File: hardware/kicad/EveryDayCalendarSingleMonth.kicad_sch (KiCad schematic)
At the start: 143 parts, among them J1_ONE_WIRE1 Conn_01x03, J2_POWER_IN1 Conn_01x02, J3_PROGRAMING_PIN1 Conn_01x06, Q1_PROGRAMING1 PN2222A, Q2_PROGRAMING1 PN2222A, U1 74AHC1G125

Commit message: Working on getting all the traces done
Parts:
- removed C12, C3: 1uF,25V,X5R, tom-passives:C_0402_1005Metric, symbol jlcpcb-basic-capacitor-0402:1uF,25V,X5R
- removed TP1_IO1: TestPoint, TestPoint:TestPoint_Pad_D2.0mm, symbol Connector:TestPoint
- added SW_WIN2: Switch_SW_Push, calendar:SW_Push_1P1T_NO_6x6mm_H9.5mm, symbol tom-mechanical:SW_SPST
- added TP_LEDLINK_IN1: TestPoint, TestPoint:TestPoint_Pad_2.5x2.5mm, symbol Connector:TestPoint
- renumbered C20 to C19, C21 to C20, C22 to C21, C23 to C22, C24 to C23, C25 to C24, C26 to C25, C27 to C26, C28 to C27, C29 to C28, C30 to C29, C31 to C30, C32 to C31, C33 to C32, C34 to C33, C35 to C34, C36 to C35, C37 to C36, C38 to C37, C39 to C38, C40 to C39, C41 to C40, C42 to C41, C43 to C42, C50 to C43, D19 to D1, D1 to DAY1, D10 to DAY10, D11 to DAY11, D12 to DAY12, D13 to DAY13, D14 to DAY14, D15 to DAY15, D16 to DAY16, D17 to DAY17, D18 to DAY18, D20 to DAY19, D2 to DAY2, D21 to DAY20, D22 to DAY21, D23 to DAY22, D24 to DAY23, D25 to DAY24, D26 to DAY25, D27 to DAY26, D28 to DAY27, D29 to DAY28, D30 to DAY29, D3 to DAY3, D31 to DAY30, D32 to DAY31, D33 to DAY32, D34 to DAY33, D35 to DAY34, D36 to DAY35, D37 to DAY36, D38 to DAY37, D39 to DAY38, D40 to DAY39, D4 to DAY4, D41 to DAY40, D42 to DAY41, D43 to DAY42, D5 to DAY5, D6 to DAY6, D7 to DAY7, D8 to DAY8, D9 to DAY9, TP_CORNER_3 to TP_CORNER_2, TP_CORNER_4 to TP_CORNER_3, TP_CORNER_2 to TP_CORNER_4, TP1 to TP_LEDLINK_OUT1
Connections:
- net PIN_TEST_POINT is gone; now on net WEEK1: U_CPU1.26 (IO4)
- net DAY1: now also U_CPU1.13 (IO14); no longer U_CPU1.29 (IO5)
- net DAY2: now also U_CPU1.23 (IO15); no longer U_CPU1.14 (IO12)
- net DAY3: now also U_CPU1.33 (IO21); no longer U_CPU1.13 (IO14)
- net DAY4: now also U_CPU1.36 (IO22); no longer U_CPU1.23 (IO15)
- net DAY5: now also U_CPU1.37 (IO23); no longer U_CPU1.27 (IO16)
- net DAY6: now also U_CPU1.10 (IO25); no longer U_CPU1.28 (IO17)
- net DAY7: now also U_CPU1.11 (IO26); no longer U_CPU1.30 (IO18)
- net GND: now also SW_WIN2.1 (A)
- net PIN_LED_CAL: now also U_CPU1.14 (IO12); no longer U_CPU1.9 (IO33)
- net WEEK1: no longer U_CPU1.31 (IO19)
- net WEEK2: now also U_CPU1.27 (IO16); no longer U_CPU1.33 (IO21)
- net WEEK3: now also U_CPU1.28 (IO17); no longer U_CPU1.36 (IO22)
- net WEEK4: now also U_CPU1.29 (IO5); no longer U_CPU1.37 (IO23)
- net WEEK5: now also U_CPU1.31 (IO19); no longer U_CPU1.10 (IO25)
- net WEEK6: now also U_CPU1.30 (IO18); no longer U_CPU1.11 (IO26)
- net at D_S1.3 (DIN): now also DAY42.1 (DOUT); no longer U1.4
- net at DAY1.3 (DIN): now also U1.4; no longer D_S3.1 (DOUT)
- net at TP_LEDLINK_OUT1.1: now also D_S3.1 (DOUT); no longer DAY42.1 (DOUT)
- net BUTTON_WIN renamed BUTTON_WIN1
- net LED_LINK: no longer names the net of R1.2, U1.2
- net LED_LINK: now also TP_LEDLINK_IN1.1
- new net BUTTON_WIN2: SW_WIN2.2 (B), U_CPU1.9 (IO33)
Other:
- moved on the sheet: C13, C14, C15, C16, C17, C18, C19, C20, C21, C22, C23, C24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

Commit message: added GND base
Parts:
- removed TP_CORNER_1, TP_CORNER_2, TP_CORNER_3, TP_CORNER_4: TestPoint, MountingHole:MountingHole_3.2mm_M3, symbol Connector:TestPoint
- renumbered SW_RESET_PROGRAMING1 to SW_BOOTLOAD1
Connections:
- net VCC is gone; now on net +5V: U1.5 (VCC)
- net RESET: now also SW_RESET1.1 (A)
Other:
- note removed: "TODO: Fix power to U2"

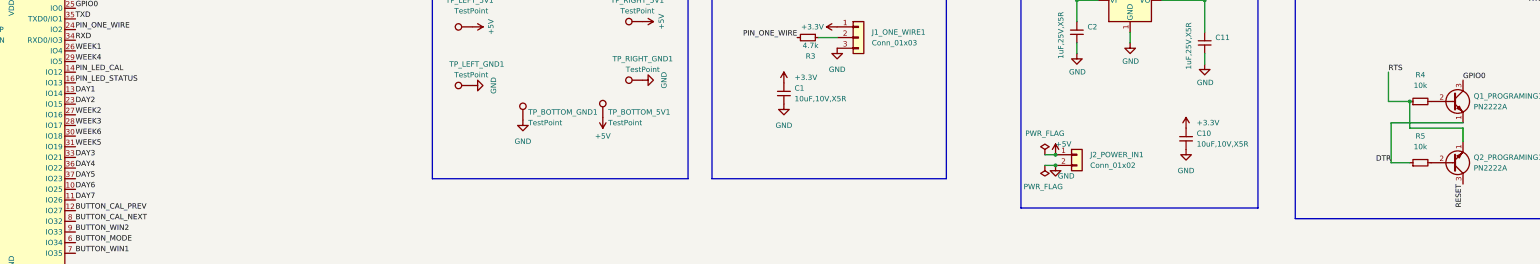
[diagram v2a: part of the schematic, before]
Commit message: Added 3d part for pushbuttons
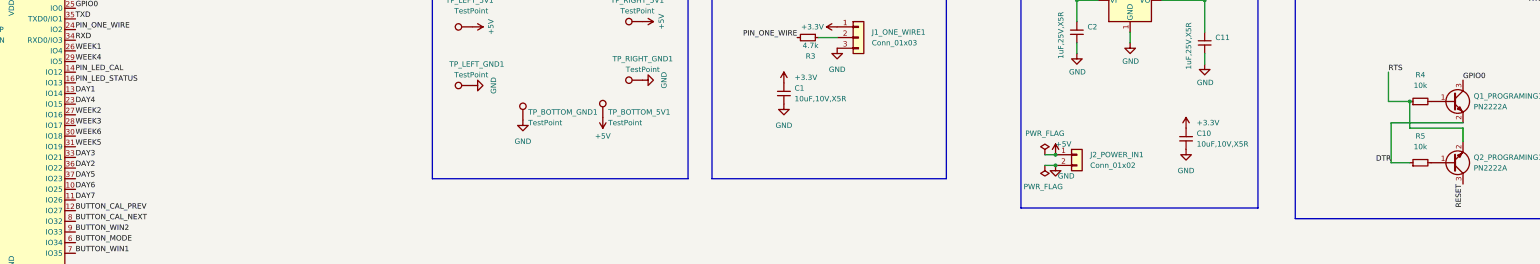
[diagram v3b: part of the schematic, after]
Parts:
- Q1_PROGRAMING1, Q2_PROGRAMING1: symbol Transistor_BJT:PN2222A -> Transistor_BJT:MMBT3904
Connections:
- net DAY2: now also U_CPU1.36 (IO22); no longer U_CPU1.23 (IO15)
- net DAY4: now also U_CPU1.23 (IO15); no longer U_CPU1.36 (IO22)
- net DTR: now also Q1_PROGRAMING1.2 (E); no longer Q1_PROGRAMING1.1 (E)
- net RTS: now also Q2_PROGRAMING1.2 (E); no longer Q2_PROGRAMING1.1 (E)
- net at R4.2: now also Q1_PROGRAMING1.1 (B); no longer Q1_PROGRAMING1.2 (B)
- net at R5.2: now also Q2_PROGRAMING1.1 (B); no longer Q2_PROGRAMING1.2 (B)
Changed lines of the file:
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@@
     (effects (font (size 1.27 1.27)) (justify left bottom))
   )
-  (label "DAY4" (at 137.795 104.775 0)
+  (label "DAY4" (at 137.795 89.535 0)
     (effects (font (size 1.27 1.27)) (justify left bottom))
   )
@@
     (effects (font (size 1.27 1.27)) (justify left bottom))
   )
-  (label "DAY2" (at 137.795 89.535 0)
+  (label "DAY2" (at 137.795 104.775 0)
     (effects (font (size 1.27 1.27)) (justify left bottom))
   )
@@
     (pin "4")
   )
-  (symbol (lib_id "Transistor_BJT:PN2222A") (at 466.09 103.505 0) (mirror x) (unit 1)
+  (symbol (lib_id "Transistor_BJT:MMBT3904") (at 466.09 103.505 0) (mirror x) (unit 1)
     (in_bom yes) (on_board yes) (fields_autoplaced)
     (property "Reference" "Q2_PROGRAMING1" (id 0) (at 471.17 102.2349 0)
@@
       (effects (font (size 1.27 1.27) italic) (justify left) hide)
     )
-    (property "Datasheet" "https://www.onsemi.com/pub/Collateral/PN2222-D.PDF" (id 3) (at 466.09 103.505 0)
+    (property "Datasheet" "https://www.onsemi.com/pub/Collateral/2N3903-D.PDF" (id 3) (at 466.09 103.505 0)
       (effects (font (size 1.27 1.27)) (justify left) hide)
     )
@@
     (pin "1")
   )
-  (symbol (lib_id "Transistor_BJT:PN2222A") (at 466.09 88.9 0) (unit 1)
+  (symbol (lib_id "Transistor_BJT:MMBT3904") (at 466.09 88.9 0) (unit 1)
     (in_bom yes) (on_board yes) (fields_autoplaced)
     (property "Reference" "Q1_PROGRAMING1" (id 0) (at 471.17 87.6299 0)
@@
       (effects (font (size 1.27 1.27) italic) (justify left) hide)
     )
-    (property "Datasheet" "https://www.onsemi.com/pub/Collateral/PN2222-D.PDF" (id 3) (at 466.09 88.9 0)
+    (property "Datasheet" "https://www.onsemi.com/pub/Collateral/2N3903-D.PDF" (id 3) (at 466.09 88.9 0)
       (effects (font (size 1.27 1.27)) (justify left) hide)
     )

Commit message: Zero errors or warnings.
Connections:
- net +3.3V: no longer C1.1, J1_ONE_WIRE1.1 (Pin_1)
- net +5V: now also C1.1, J1_ONE_WIRE1.1 (Pin_1)
- net BUTTON_CAL_NEXT: now also U_CPU1.6 (IO34); no longer U_CPU1.8 (IO32)
- net BUTTON_CAL_PREV: now also U_CPU1.7 (IO35); no longer U_CPU1.12 (IO27)
- net BUTTON_MODE: now also U_CPU1.8 (IO32); no longer U_CPU1.6 (IO34)
- net BUTTON_WIN1: now also U_CPU1.11 (IO26); no longer U_CPU1.7 (IO35)
- net DAY1: now also U_CPU1.37 (IO23); no longer U_CPU1.13 (IO14)
- net DAY5: now also U_CPU1.14 (IO12); no longer U_CPU1.37 (IO23)
- net DAY6: now also U_CPU1.13 (IO14); no longer U_CPU1.10 (IO25)
- net DAY7: now also U_CPU1.12 (IO27); no longer U_CPU1.11 (IO26)
- net PIN_LED_CAL: now also U_CPU1.10 (IO25); no longer U_CPU1.14 (IO12)
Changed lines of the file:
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@@
     (effects (font (size 1.27 1.27)) (justify left bottom))
   )
-  (label "BUTTON_CAL_NEXT" (at 137.795 117.475 0)
+  (label "BUTTON_CAL_NEXT" (at 137.795 122.555 0)
     (effects (font (size 1.27 1.27)) (justify left bottom))
   )
@@
     (effects (font (size 1.27 1.27)) (justify left bottom))
   )
-  (label "DAY5" (at 137.795 107.315 0)
+  (label "DAY5" (at 137.795 81.915 0)
     (effects (font (size 1.27 1.27)) (justify left bottom))
   )
@@
     (effects (font (size 1.27 1.27)) (justify right bottom))
   )
-  (label "DAY6" (at 137.795 109.855 0)
+  (label "DAY6" (at 137.795 86.995 0)
     (effects (font (size 1.27 1.27)) (justify left bottom))
   )
@@
     (effects (font (size 1.27 1.27)) (justify left bottom))
   )
-  (label "BUTTON_WIN1" (at 137.795 125.095 0)
+  (label "BUTTON_WIN1" (at 137.795 112.395 0)
     (effects (font (size 1.27 1.27)) (justify left bottom))
   )
@@
     (effects (font (size 1.27 1.27)) (justify left bottom))
   )
-  (label "BUTTON_MODE" (at 137.795 122.555 0)
+  (label "BUTTON_MODE" (at 137.795 117.475 0)
     (effects (font (size 1.27 1.27)) (justify left bottom))
   )
-  (label "DAY1" (at 137.795 86.995 0)
+  (label "DAY1" (at 137.795 107.315 0)
     (effects (font (size 1.27 1.27)) (justify left bottom))
   )
@@
     (effects (font (size 1.27 1.27)) (justify right bottom))
   )
-  (label "DAY7" (at 137.795 112.395 0)
+  (label "DAY7" (at 137.795 114.935 0)
     (effects (font (size 1.27 1.27)) (justify left bottom))
   )
@@
     (effects (font (size 1.27 1.27)) (justify right bottom))
   )
-  (label "BUTTON_CAL_PREV" (at 137.795 114.935 0)
+  (label "BUTTON_CAL_PREV" (at 137.795 125.095 0)
     (effects (font (size 1.27 1.27)) (justify left bottom))
   )
-  (label "PIN_LED_CAL" (at 137.795 81.915 0)
+  (label "PIN_LED_CAL" (at 137.795 109.855 0)
     (effects (font (size 1.27 1.27)) (justify left bottom))
   )
@@
     (pin "1")
   )
-  (symbol (lib_id "power:+3.3V") (at 319.405 71.12 90) (unit 1)
-    (in_bom yes) (on_board yes) (fields_autoplaced)
-    (property "Reference" "#PWR010" (id 0) (at 323.215 71.12 0)
-      (effects (font (size 1.27 1.27)) hide)
-    )
-    (property "Value" "+3.3V" (id 1) (at 316.23 71.1199 90)
-      (effects (font (size 1.27 1.27)) (justify left))
-    )
-    (property "Footprint" "" (id 2) (at 319.405 71.12 0)
-      (effects (font (size 1.27 1.27)) hide)
-    )
-    (property "Datasheet" "" (id 3) (at 319.405 71.12 0)
-      (effects (font (size 1.27 1.27)) hide)
-    )
-    (pin "1")
-  )
   (symbol (lib_id "calendar:WS2812B") (at 243.84 238.125 0) (unit 1)
     (in_bom yes) (on_board yes) (fields_autoplaced)
@@
     (pin "3")
   )
+  (symbol (lib_id "power:+5V") (at 306.705 84.455 0) (unit 1)
+    (in_bom yes) (on_board yes) (fields_autoplaced)
+    (property "Reference" "#PWR08" (id 0) (at 306.705 88.265 0)
+      (effects (font (size 1.27 1.27)) hide)
+    )
+    (property "Value" "+5V" (id 1) (at 306.705 79.375 0))
+    (property "Footprint" "" (id 2) (at 306.705 84.455 0)
+      (effects (font (size 1.27 1.27)) hide)
+    )
+    (property "Datasheet" "" (id 3) (at 306.705 84.455 0)
+      (effects (font (size 1.27 1.27)) hide)
+    )
+    (pin "1")
+  )
   (symbol (lib_id "tom-mechanical:SW_SPST") (at 38.1 71.12 0) (unit 1)
     (in_bom yes) (on_board yes)
@@
     (pin "2")
   )
+  (symbol (lib_id "power:+5V") (at 319.405 71.12 0) (unit 1)
+    (in_bom yes) (on_board yes) (fields_autoplaced)
+    (property "Reference" "#PWR010" (id 0) (at 319.405 74.93 0)
+      (effects (font (size 1.27 1.27)) hide)
+    )
+    (property "Value" "+5V" (id 1) (at 319.405 66.04 0))
+    (property "Footprint" "" (id 2) (at 319.405 71.12 0)
+      (effects (font (size 1.27 1.27)) hide)
+    )
+    (property "Datasheet" "" (id 3) (at 319.405 71.12 0)
+      (effects (font (size 1.27 1.27)) hide)
+    )
+    (pin "1")
+  )
   (symbol (lib_id "calendar:WS2812B") (at 193.04 194.945 0) (unit 1)
     (in_bom yes) (on_board yes) (fields_autoplaced)
@@
     (pin "1")
   )
-  (symbol (lib_id "power:+3.3V") (at 306.705 84.455 0) (unit 1)
-    (in_bom yes) (on_board yes) (fields_autoplaced)
-    (property "Reference" "#PWR08" (id 0) (at 306.705 88.265 0)
-      (effects (font (size 1.27 1.27)) hide)
-    )
-    (property "Value" "+3.3V" (id 1) (at 309.245 83.1849 0)
-      (effects (font (size 1.27 1.27)) (justify left))
-    )
-    (property "Footprint" "" (id 2) (at 306.705 84.455 0)
-      (effects (font (size 1.27 1.27)) hide)
-    )
-    (property "Datasheet" "" (id 3) (at 306.705 84.455 0)
-      (effects (font (size 1.27 1.27)) hide)
-    )
-    (pin "1")
-  )
   (symbol (lib_id "power:+3.3V") (at 532.13 103.505 0) (unit 1)
     (in_bom yes) (on_board yes) (fields_autoplaced)
@@
       (reference "#PWR07") (unit 1) (value "GND") (footprint "")
     )
-    (path "/ef50650b-f40e-490b-b982-9f1bf0858617"
-      (reference "#PWR08") (unit 1) (value "+3.3V") (footprint "")
+    (path "/d2220ca1-4a38-4f7e-9c73-e0b2c3831917"
+      (reference "#PWR08") (unit 1) (value "+5V") (footprint "")
     )
     (path "/67f5eb89-5a5c-4633-8502-1c1dd8c84ae3"
       (reference "#PWR09") (unit 1) (value "GND") (footprint "")
     )
-    (path "/c3bbb8f7-f74d-4bf2-b28f-3f9ca4cf3c15"
-      (reference "#PWR010") (unit 1) (value "+3.3V") (footprint "")
+    (path "/d4519b1b-f257-451e-827a-277f5ee80280"
+      (reference "#PWR010") (unit 1) (value "+5V") (footprint "")
     )
     (path "/b35a029b-6727-4ae4-bcd0-21bab0a3bb4a"

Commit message: Updated silkscreen
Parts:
- renumbered TP_BOTTOM_5V1 to 5V, TP_RIGHT_5V1 to 5V, TP_LEFT_5V1 to 5V, SW_CAL_NEXT1 to CAL_NEXT, TP_BOTTOM_GND1 to GND, TP_LEDLINK_IN1 to LED_IN, TP_LEDLINK_OUT1 to LED_OUT, J1_ONE_WIRE1 to ONE_WIRE, Q1_PROGRAMING1 to Q1, Q2_PROGRAMING1 to Q2
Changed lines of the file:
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@@
   (symbol (lib_id "tom-mechanical:SW_SPST") (at 36.195 236.855 0) (unit 1)
     (in_bom yes) (on_board yes)
-    (property "Reference" "SW_CAL_NEXT1" (id 0) (at 36.195 231.14 0))
+    (property "Reference" "CAL_NEXT" (id 0) (at 36.195 231.14 0))
     (property "Value" "Switch_SW_Push" (id 1) (at 36.195 233.4514 0))
     (property "Footprint" "calendar:SW_Push_1P1T_NO_6x6mm_H9.5mm" (id 2) (at 36.195 231.775 0)
@@
   (symbol (lib_id "Transistor_BJT:MMBT3904") (at 466.09 103.505 0) (mirror x) (unit 1)
     (in_bom yes) (on_board yes) (fields_autoplaced)
-    (property "Reference" "Q2_PROGRAMING1" (id 0) (at 471.17 102.2349 0)
+    (property "Reference" "Q2" (id 0) (at 471.17 102.2349 0)
       (effects (font (size 1.27 1.27)) (justify left))
     )
@@
   (symbol (lib_id "Connector:TestPoint") (at 263.525 92.71 0) (unit 1)
     (in_bom yes) (on_board yes)
-    (property "Reference" "TP_BOTTOM_5V1" (id 0) (at 264.795 91.44 0)
+    (property "Reference" "5V" (id 0) (at 264.795 91.44 0)
       (effects (font (size 1.27 1.27)) (justify left))
     )
@@
   (symbol (lib_id "Connector:TestPoint") (at 273.05 69.85 90) (mirror x) (unit 1)
     (in_bom yes) (on_board yes)
-    (property "Reference" "TP_RIGHT_5V1" (id 0) (at 271.78 64.77 90))
+    (property "Reference" "5V" (id 0) (at 271.78 64.77 90))
     (property "Value" "TestPoint" (id 1) (at 271.78 67.31 90))
     (property "Footprint" "TestPoint:TestPoint_Pad_2.5x2.5mm" (id 2) (at 273.05 74.93 0)
@@
   (symbol (lib_id "Connector:TestPoint") (at 226.06 330.2 180) (unit 1)
     (in_bom yes) (on_board yes) (fields_autoplaced)
-    (property "Reference" "TP_LEDLINK_OUT1" (id 0) (at 227.965 332.2319 0)
+    (property "Reference" "LED_OUT" (id 0) (at 227.965 332.2319 0)
       (effects (font (size 1.27 1.27)) (justify right))
     )
@@
   (symbol (lib_id "Connector:TestPoint") (at 244.475 93.345 0) (unit 1)
     (in_bom yes) (on_board yes)
-    (property "Reference" "TP_BOTTOM_GND1" (id 0) (at 245.745 91.44 0)
+    (property "Reference" "GND" (id 0) (at 245.745 91.44 0)
       (effects (font (size 1.27 1.27)) (justify left))
     )
@@
   (symbol (lib_id "Connector:TestPoint") (at 129.54 173.355 180) (unit 1)
     (in_bom yes) (on_board yes)
-    (property "Reference" "TP_LEDLINK_IN1" (id 0) (at 128.27 179.07 0)
+    (property "Reference" "LED_IN" (id 0) (at 128.27 179.07 0)
       (effects (font (size 1.27 1.27)) (justify left))
     )
@@
   (symbol (lib_id "Transistor_BJT:MMBT3904") (at 466.09 88.9 0) (unit 1)
     (in_bom yes) (on_board yes) (fields_autoplaced)
-    (property "Reference" "Q1_PROGRAMING1" (id 0) (at 471.17 87.6299 0)
+    (property "Reference" "Q1" (id 0) (at 471.17 87.6299 0)
       (effects (font (size 1.27 1.27)) (justify left))
     )
@@
   (symbol (lib_id "Connector:TestPoint") (at 232.41 71.12 90) (unit 1)
     (in_bom yes) (on_board yes)
-    (property "Reference" "TP_LEFT_5V1" (id 0) (at 237.49 64.77 90)
+    (property "Reference" "5V" (id 0) (at 237.49 64.77 90)
       (effects (font (size 1.27 1.27)) (justify left))
     )
@@
   (symbol (lib_id "Connector_Generic:Conn_01x03") (at 324.485 73.66 0) (unit 1)
     (in_bom yes) (on_board yes) (fields_autoplaced)
-    (property "Reference" "J1_ONE_WIRE1" (id 0) (at 327.66 72.3899 0)
+    (property "Reference" "ONE_WIRE" (id 0) (at 327.66 72.3899 0)
       (effects (font (size 1.27 1.27)) (justify left))
     )
@@
       (reference "#PWR055") (unit 1) (value "+5V") (footprint "")
     )
+    (path "/32b46005-ffe7-4b2f-95ab-039506cdc1b7"
+      (reference "5V") (unit 1) (value "TestPoint") (footprint "TestPoint:TestPoint_Pad_2.5x2.5mm")
+    )
+    (path "/3c88e646-5c38-44c0-8ccf-1f487b84aebb"
+      (reference "5V") (unit 1) (value "TestPoint") (footprint "TestPoint:TestPoint_Pad_2.5x2.5mm")
+    )
+    (path "/c2fa4bb1-f04a-4a45-9656-6b3c72f0c28a"
+      (reference "5V") (unit 1) (value "TestPoint") (footprint "TestPoint:TestPoint_Pad_2.5x2.5mm")
+    )
     (path "/5e5ca5be-5de2-4ecc-85e6-8fbbed803745"
       (reference "C1") (unit 1) (value "10uF,10V,X5R ") (footprint "tom-passives:C_0603_1608Metric")
@@
       (reference "C43") (unit 1) (value "1uF,25V,X5R ") (footprint "tom-passives:C_0402_1005Metric")
     )
+    (path "/1b06ff24-2237-45c9-812b-4b606d4d146a"
+      (reference "CAL_NEXT") (unit 1) (value "Switch_SW_Push") (footprint "calendar:SW_Push_1P1T_NO_6x6mm_H9.5mm")
+    )
     (path "/8e2a9caa-69a7-418c-8add-2cd62ed745dc"
       (reference "C_ROW1") (unit 1) (value "10uF,10V,X5R ") (footprint "tom-passives:C_0603_1608Metric")
@@
       (reference "D_S3") (unit 1) (value "WS2812B") (footprint "calendar:LED_WS2812C-2020-V1_2.0x2.0mm")
     )
-    (path "/d14bd5d6-1332-4c0c-b6ef-8f16c66dc11f"
-      (reference "J1_ONE_WIRE1") (unit 1) (value "Conn_01x03") (footprint "Connector_PinHeader_2.54mm:PinHeader_1x03_P2.54mm_Vertical")
+    (path "/7b5cd6f3-f591-4c08-b5a5-39d81918f5fc"
+      (reference "GND") (unit 1) (value "TestPoint") (footprint "TestPoint:TestPoint_Pad_2.5x2.5mm")
     )
     (path "/8bbc953d-12b2-4e6b-87b4-2064c0f15b50"
@@
       (reference "J3_PROGRAMING_PIN1") (unit 1) (value "Conn_01x06") (footprint "Connector_PinHeader_2.54mm:PinHeader_1x06_P2.54mm_Vertical")
     )
+    (path "/7d535c57-26b3-4d48-87e7-7f8db2eeb930"
+      (reference "LED_IN") (unit 1) (value "TestPoint") (footprint "TestPoint:TestPoint_Pad_2.5x2.5mm")
+    )
+    (path "/6dd7985d-dca0-41e4-ab7c-21fbfe33a081"
+      (reference "LED_OUT") (unit 1) (value "TestPoint") (footprint "TestPoint:TestPoint_Pad_2.5x2.5mm")
+    )
+    (path "/d14bd5d6-1332-4c0c-b6ef-8f16c66dc11f"
+      (reference "ONE_WIRE") (unit 1) (value "Conn_01x03") (footprint "Connector_PinHeader_2.54mm:PinHeader_1x03_P2.54mm_Vertical")
+    )
     (path "/ac54c097-a30f-4633-8dc5-321bb13c9afe"
-      (reference "Q1_PROGRAMING1") (unit 1) (value "PN2222A") (footprint "Package_TO_SOT_SMD:SOT-23")
+      (reference "Q1") (unit 1) (value "PN2222A") (footprint "Package_TO_SOT_SMD:SOT-23")
     )
     (path "/27175b01-f5c2-49d3-a0ee-fe570424005b"
-      (reference "Q2_PROGRAMING1") (unit 1) (value "PN2222A") (footprint "Package_TO_SOT_SMD:SOT-23")
+      (reference "Q2") (unit 1) (value "PN2222A") (footprint "Package_TO_SOT_SMD:SOT-23")
     )
     (path "/381f13c1-d635-4de7-8de0-848cc86a7093"
@@
       (reference "SW_CAL_MODE1") (unit 1) (value "Switch_SW_Push") (footprint "calendar:SW_Push_1P1T_NO_6x6mm_H9.5mm")
     )
-    (path "/1b06ff24-2237-45c9-812b-4b606d4d146a"
-      (reference "SW_CAL_NEXT1") (unit 1) (value "Switch_SW_Push") (footprint "calendar:SW_Push_1P1T_NO_6x6mm_H9.5mm")
-    )
     (path "/befa23ae-69ac-4c39-b4f3-94ed728669a7"
       (reference "SW_CAL_PREV1") (unit 1) (value "Switch_SW_Push") (footprint "calendar:SW_Push_1P1T_NO_6x6mm_H9.5mm")
@@
       (reference "SW_WIN2") (unit 1) (value "Switch_SW_Push") (footprint "calendar:SW_Push_1P1T_NO_6x6mm_H9.5mm")
     )
-    (path "/32b46005-ffe7-4b2f-95ab-039506cdc1b7"
-      (reference "TP_BOTTOM_5V1") (unit 1) (value "TestPoint") (footprint "TestPoint:TestPoint_Pad_2.5x2.5mm")
-    )
-    (path "/7b5cd6f3-f591-4c08-b5a5-39d81918f5fc"
-      (reference "TP_BOTTOM_GND1") (unit 1) (value "TestPoint") (footprint "TestPoint:TestPoint_Pad_2.5x2.5mm")
-    )
-    (path "/7d535c57-26b3-4d48-87e7-7f8db2eeb930"
-      (reference "TP_LEDLINK_IN1") (unit 1) (value "TestPoint") (footprint "TestPoint:TestPoint_Pad_2.5x2.5mm")
-    )
-    (path "/6dd7985d-dca0-41e4-ab7c-21fbfe33a081"
-      (reference "TP_LEDLINK_OUT1") (unit 1) (value "TestPoint") (footprint "TestPoint:TestPoint_Pad_2.5x2.5mm")
-    )
-    (path "/c2fa4bb1-f04a-4a45-9656-6b3c72f0c28a"
-      (reference "TP_LEFT_5V1") (unit 1) (value "TestPoint") (footprint "TestPoint:TestPoint_Pad_2.5x2.5mm")
-    )
     (path "/ef35c61f-ddc4-4b83-93cd-283cfd2965c6"
       (reference "TP_LEFT_GND1") (unit 1) (value "TestPoint") (footprint "TestPoint:TestPoint_Pad_2.5x2.5mm")
     )
-    (path "/3c88e646-5c38-44c0-8ccf-1f487b84aebb"
-      (reference "TP_RIGHT_5V1") (unit 1) (value "TestPoint") (footprint "TestPoint:TestPoint_Pad_2.5x2.5mm")
-    )
     (path "/37b33f1b-aa00-4047-9d53-2621fe291352"
